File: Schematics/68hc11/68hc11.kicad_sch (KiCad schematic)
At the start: 8 parts, among them U1 MC68HC11A1CC-PLLC, U2 74HC245, U3 74HC373, U4 27C64, U5 HM62256BLP, U6 27C64, U7 MC68B21

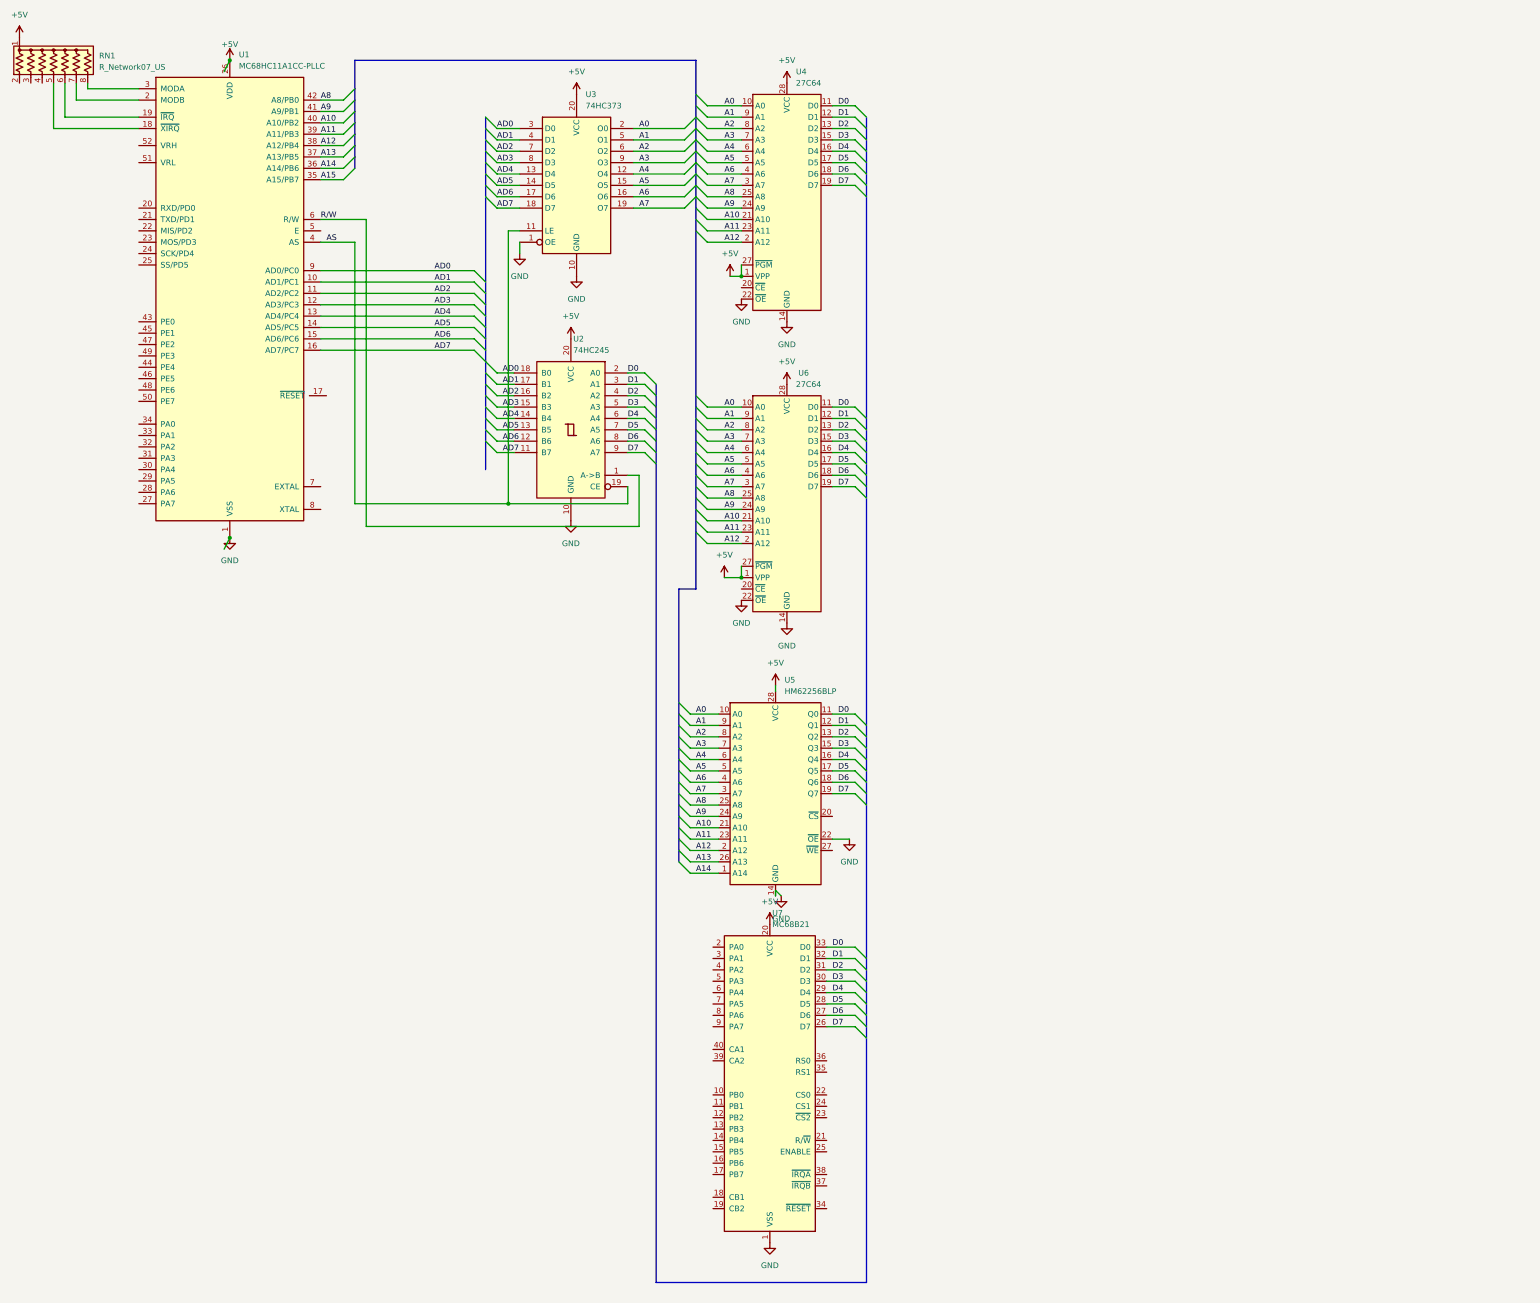
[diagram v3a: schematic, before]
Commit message: Added MAX232 and DB9 for serial comms
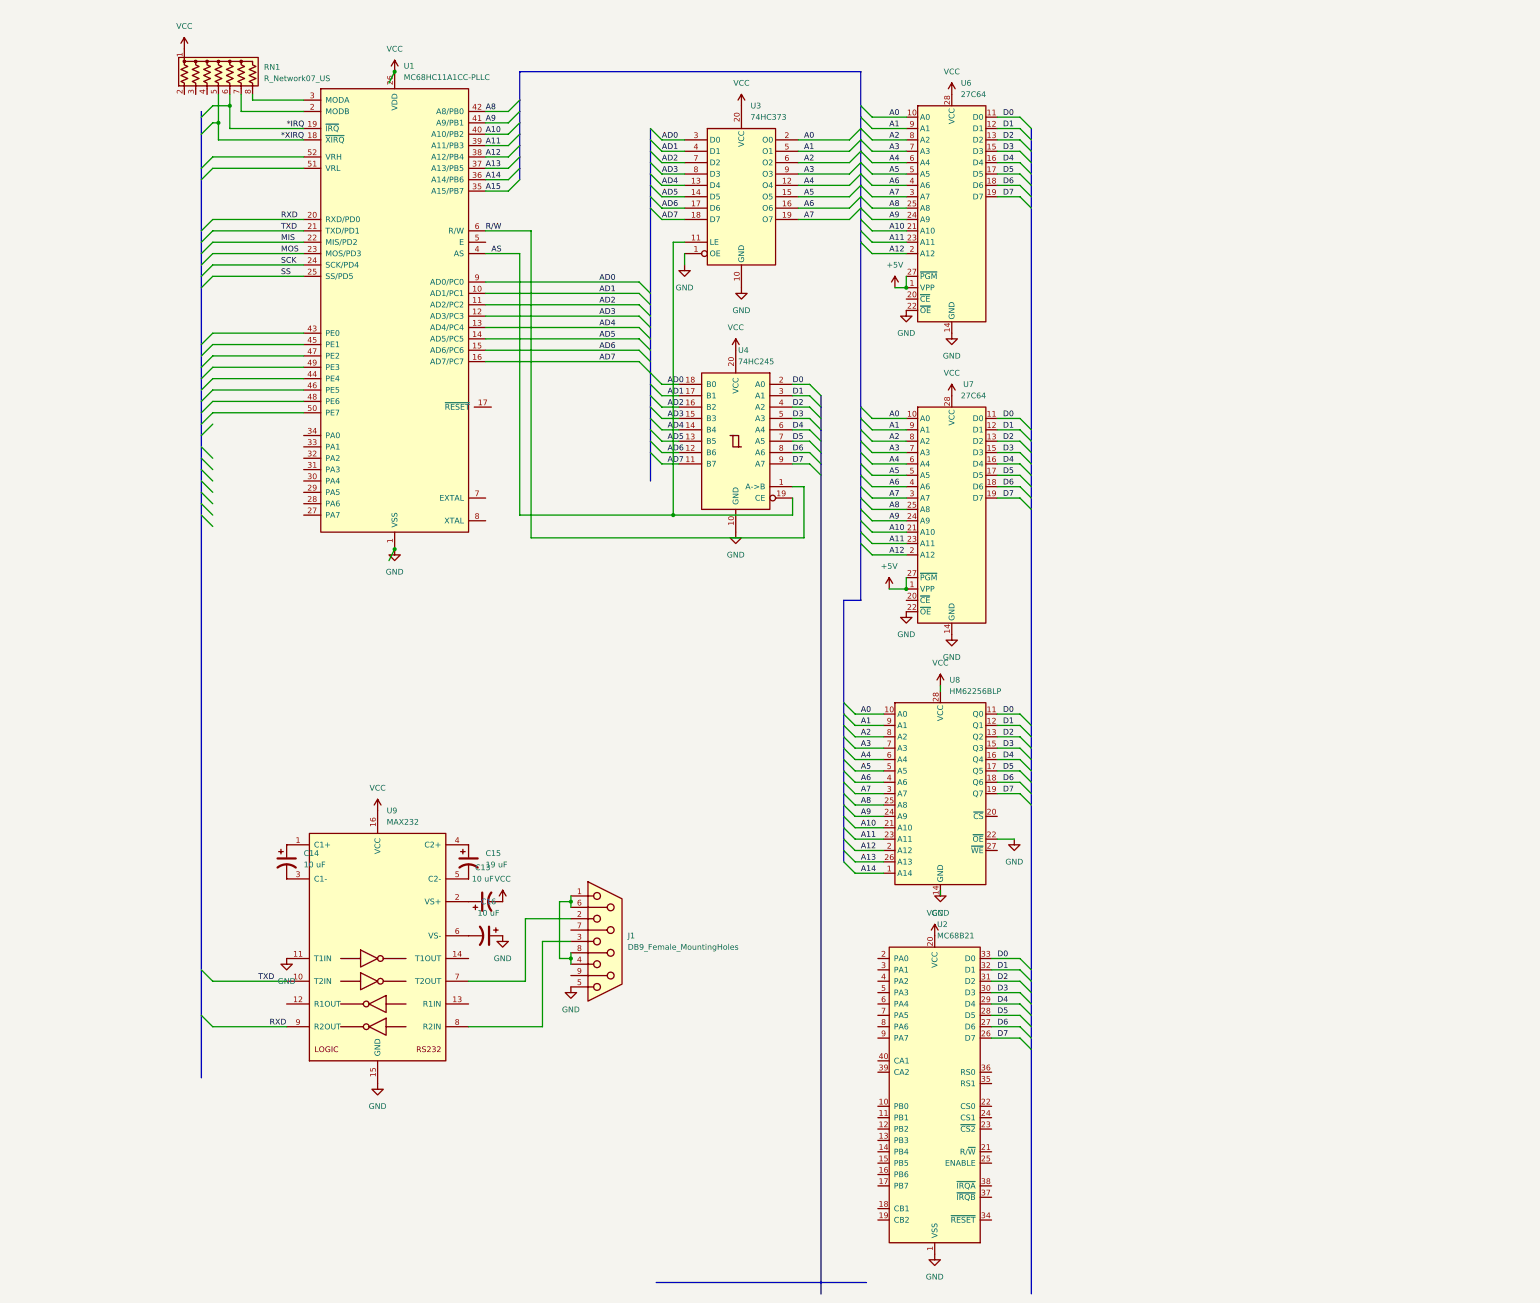
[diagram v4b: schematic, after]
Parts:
- added C13, C14, C16: 10 uF, Capacitor_THT:CP_Radial_D10.0mm_P5.00mm, symbol Device:C_Polarized_US
- added C15: 19 uF, Capacitor_THT:CP_Radial_D10.0mm_P5.00mm, symbol Device:C_Polarized_US
- added J1: DB9_Female_MountingHoles, Connector_Dsub:DSUB-9_Male_Horizontal_P2.77x2.54mm_EdgePinOffset9.40mm, symbol Connector:DB9_Female_MountingHoles
- added U9: MAX232, Package_DIP:DIP-16_W7.62mm_Socket, symbol Interface_UART:MAX232
- U2: renamed from U7; footprint Package_DIP:DIP-40_W15.24mm -> Package_DIP:DIP-40_W15.24mm_Socket
- U6: renamed from U4; footprint Package_DIP:DIP-28_W15.24mm -> Package_DIP:DIP-28_W15.24mm_Socket
- U7: renamed from U6; footprint Package_DIP:DIP-28_W15.24mm -> Package_DIP:DIP-28_W15.24mm_Socket
- U8: renamed from U5; footprint Package_DIP:DIP-28_W15.24mm -> Package_DIP:DIP-28_W15.24mm_Socket
- renumbered U2 to U4
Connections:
- net +5V: no longer RN1.1 (common), U1.26 (VDD), U2.20 (VCC), U3.20 (VCC), U4.20 (VCC), U6.28 (VCC), U7.28 (VCC), U8.28 (VCC)
- net GND: now also C16.1, J1.5, U9.11 (T1IN), U9.15 (GND)
- net *XIRQ: now reaches RN1.5 (R4), U1.18 (~{XIRQ})
- net *IRQ: now reaches RN1.6 (R5), U1.19 (~{IRQ})
- net RXD: now reaches U1.20 (RXD/PD0)
- net RXD: now also U9.9 (R2OUT)
- net TXD: now reaches U1.21 (TXD/PD1)
- net TXD: now also U9.10 (T2IN)
- net MIS: now reaches U1.22 (MIS/PD2)
- net MOS: now reaches U1.23 (MOS/PD3)
- net SCK: now reaches U1.24 (SCK/PD4)
- net SS: now reaches U1.25 (SS/PD5)
- new net: C15.1, U9.4 (C2+)
- new net: C15.2, U9.5 (C2-)
- new net: C14.1, U9.1 (C1+)
- new net: C14.2, U9.3 (C1-)
- new net: J1.1, J1.4, J1.6, J1.8
- new net: J1.2, U9.7 (T2OUT)
- new net: J1.3, U9.8 (R2IN)
- new net: C16.2, U9.6 (VS-)
- new net: C13.1, U9.2 (VS+)
- new net VCC: C13.2, RN1.1 (common), U1.26 (VDD), U2.20 (VCC), U3.20 (VCC), U4.20 (VCC), U6.28 (VCC), U7.28 (VCC), U8.28 (VCC), U9.16 (VCC)
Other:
- moved on the sheet: RN1, U1, U2, U3, U4, U6, U7, U8

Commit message: Added Crystal and some trace routing
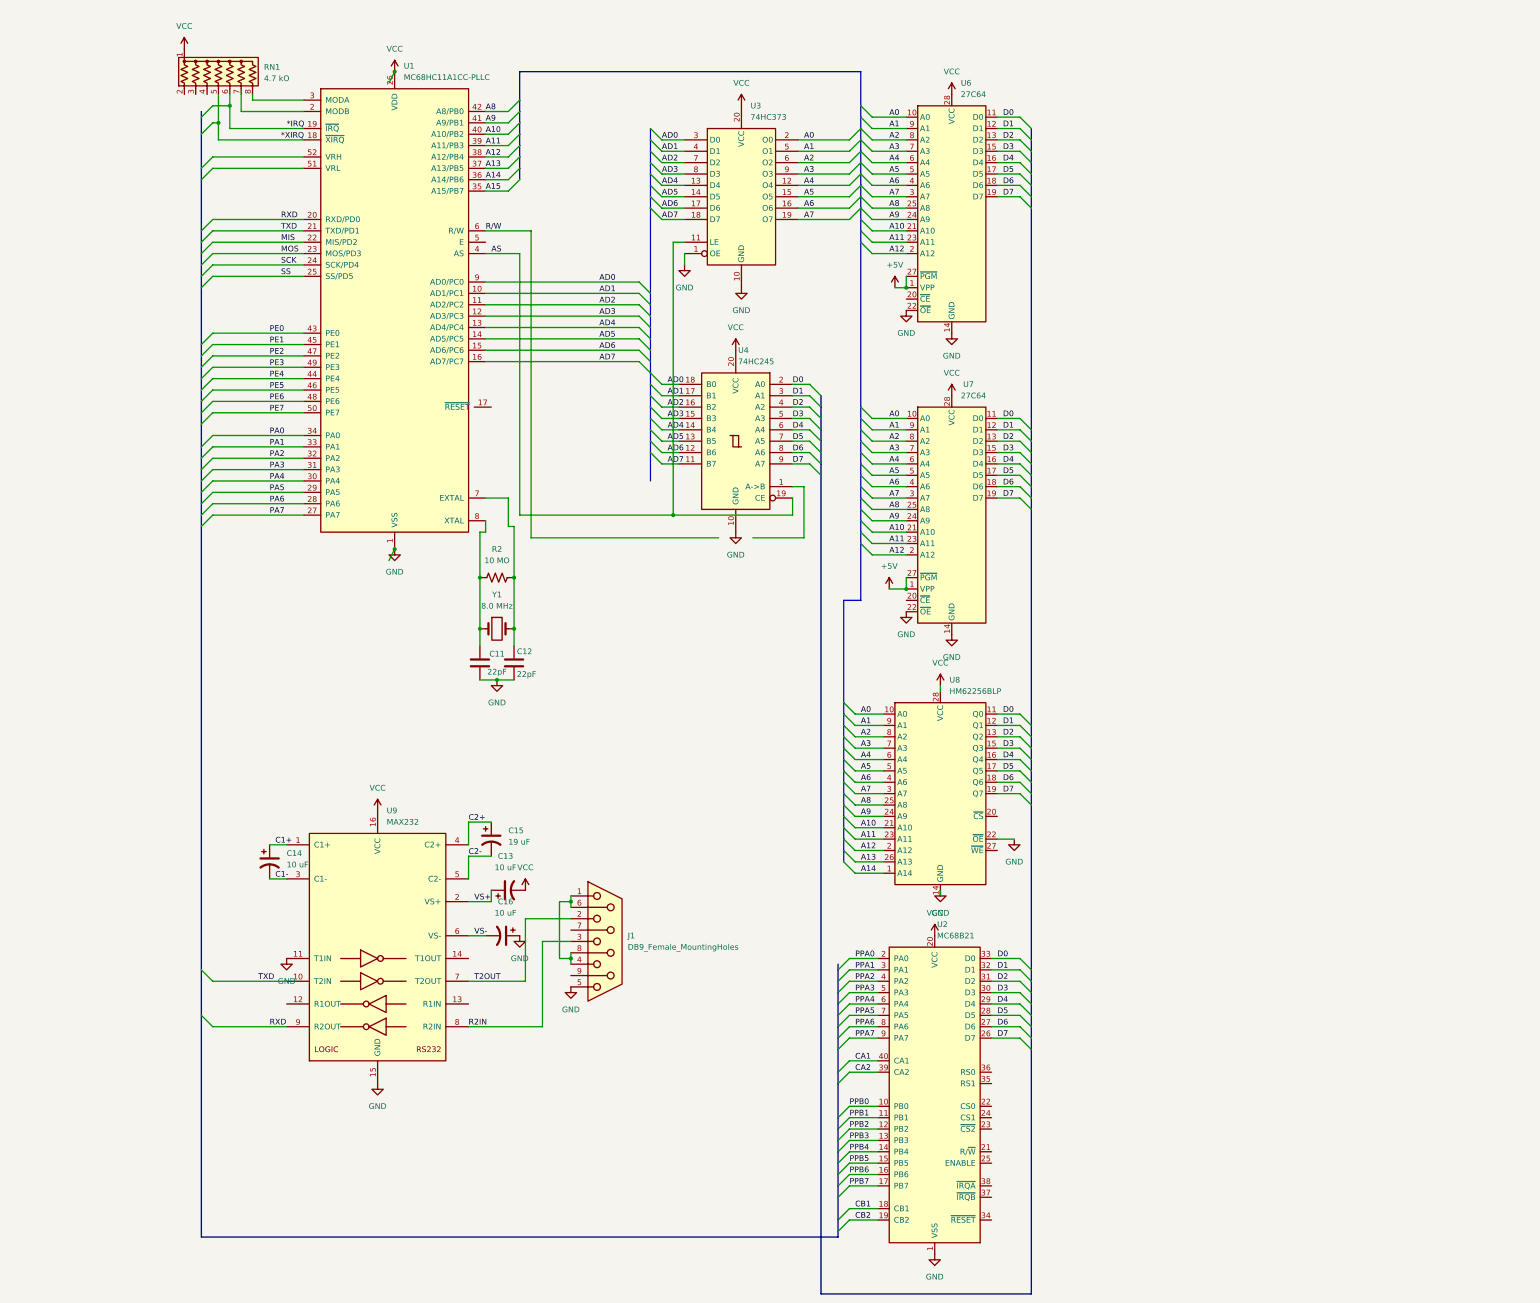
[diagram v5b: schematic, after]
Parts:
- added C11, C12: 22pF, Capacitor_THT:C_Disc_D3.0mm_W1.6mm_P2.50mm, symbol Device:C
- added R2: 10 MO, Resistor_THT:R_Axial_DIN0309_L9.0mm_D3.2mm_P12.70mm_Horizontal, symbol Device:R_US
- added Y1: 8.0 MHz, Crystal:Crystal_HC49-4H_Vertical, symbol Device:Crystal
- C13, C14, C15, C16: footprint Capacitor_THT:CP_Radial_D10.0mm_P5.00mm -> Capacitor_THT:CP_Radial_D5.0mm_P2.00mm
- RN1: value R_Network07_US -> 4.7 kO
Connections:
- net GND: now also C11.2, C12.2
- net R/W: no longer U4.1 (A->B)
- net C2+: now reaches C15.1, U9.4 (C2+)
- net C2-: now reaches C15.2, U9.5 (C2-)
- net C1+: now reaches C14.1, U9.1 (C1+)
- net C1-: now reaches C14.2, U9.3 (C1-)
- net T2OUT: now reaches J1.2, U9.7 (T2OUT)
- net R2IN: now reaches J1.3, U9.8 (R2IN)
- net PA7: now reaches U1.27 (PA7)
- net PA6: now reaches U1.28 (PA6)
- net PA5: now reaches U1.29 (PA5)
- net PA4: now reaches U1.30 (PA4)
- net PA3: now reaches U1.31 (PA3)
- net PA2: now reaches U1.32 (PA2)
- net PA1: now reaches U1.33 (PA1)
- net PA0: now reaches U1.34 (PA0)
- net PE0: now reaches U1.43 (PE0)
- net PE4: now reaches U1.44 (PE4)
- net PE1: now reaches U1.45 (PE1)
- net PE5: now reaches U1.46 (PE5)
- net PE2: now reaches U1.47 (PE2)
- net PE6: now reaches U1.48 (PE6)
- net PE3: now reaches U1.49 (PE3)
- net PE7: now reaches U1.50 (PE7)
- net at U1.7 (EXTAL): now also C12.1, R2.1, Y1.2
- net at U1.8 (XTAL): now also C11.1, R2.2, Y1.1
- net PPB0: now reaches U2.10 (PB0)
- net PPB1: now reaches U2.11 (PB1)
- net PPB2: now reaches U2.12 (PB2)
- net PPB3: now reaches U2.13 (PB3)
- net PPB4: now reaches U2.14 (PB4)
- net PPB5: now reaches U2.15 (PB5)
- net PPB6: now reaches U2.16 (PB6)
- net PPB7: now reaches U2.17 (PB7)
- net CB1: now reaches U2.18 (CB1)
- net CB2: now reaches U2.19 (CB2)
- net PPA0: now reaches U2.2 (PA0)
- net PPA1: now reaches U2.3 (PA1)
- net CA2: now reaches U2.39 (CA2)
- net PPA2: now reaches U2.4 (PA2)
- net CA1: now reaches U2.40 (CA1)
- net PPA3: now reaches U2.5 (PA3)
- net PPA4: now reaches U2.6 (PA4)
- net PPA5: now reaches U2.7 (PA5)
- net PPA6: now reaches U2.8 (PA6)
- net PPA7: now reaches U2.9 (PA7)
- net VS-: now reaches C16.2, U9.6 (VS-)
- net VS+: now reaches C13.1, U9.2 (VS+)
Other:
- moved on the sheet: C13, C14, C15, C16

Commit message: Added low power reset and cleaned up busses
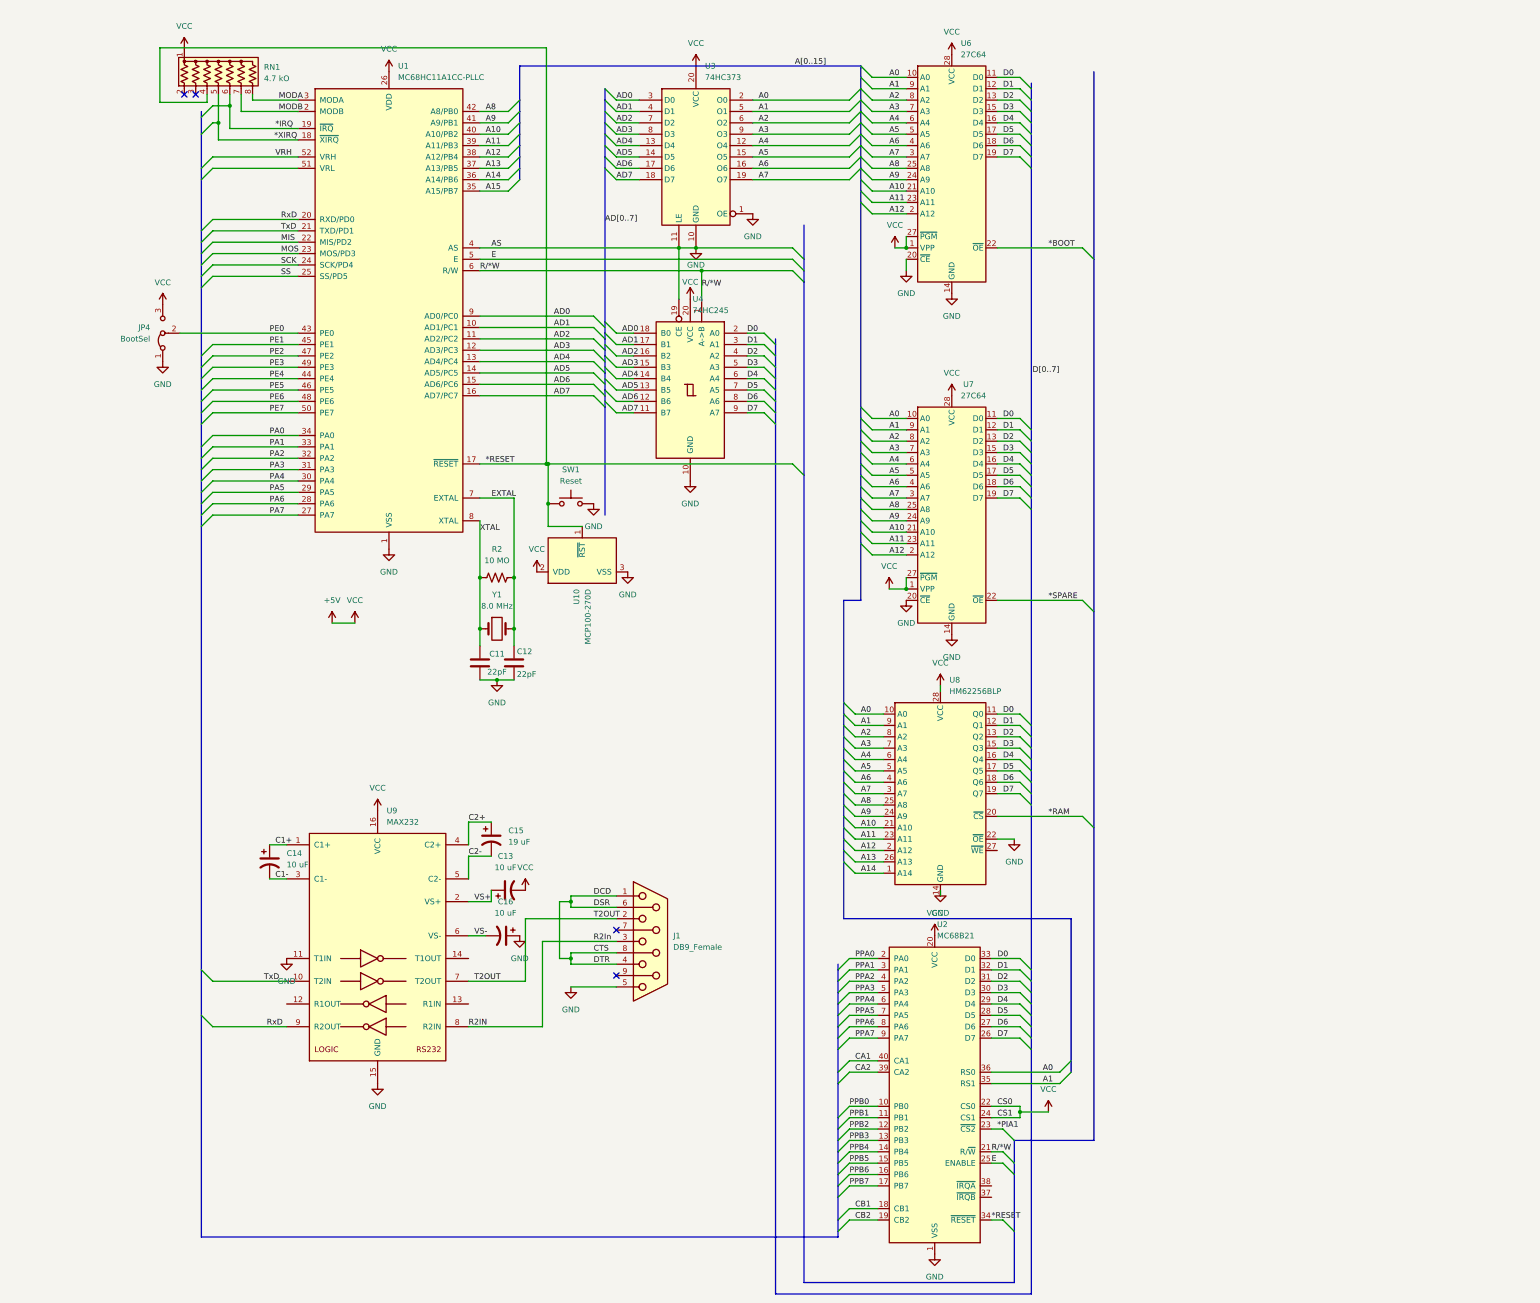
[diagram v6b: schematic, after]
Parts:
- added JP4: BootSel, Connector_PinHeader_1.00mm:PinHeader_1x03_P1.00mm_Vertical, symbol Jumper:Jumper_3_Bridged12
- added SW1: Reset, Button_Switch_THT:SW_PUSH_6mm, symbol Switch:SW_Push
- added U10: MCP100-270D, Package_TO_SOT_THT:TO-92, symbol Power_Supervisor:MCP100-270D
- J1: value DB9_Female_MountingHoles -> DB9_Female
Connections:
- net AS is gone; now on net GND: U1.4 (AS), U3.11 (LE), U4.19 (CE)
- net R/W is gone; now on net R/*W: U1.6 (R/W)
- net VCC is gone; now on net +5V: C13.2, RN1.1 (common), U1.26 (VDD), U2.20 (VCC), U3.20 (VCC), U4.20 (VCC), U6.28 (VCC), U7.28 (VCC), U8.28 (VCC), U9.16 (VCC)
- net +5V: now also U2.22 (CS0), U2.24 (CS1), JP4.3 (B), U10.2 (VDD)
- net A0: now also U2.36 (RS0)
- net A1: now also U2.35 (RS1)
- net GND: now also U6.20 (~{CE}), U7.20 (~{CE}), JP4.1 (A), SW1.2, U10.3 (VSS); no longer U6.22 (~{OE}), U7.22 (~{OE})
- net PE0: now also JP4.2 (C)
- net *RESET: now reaches RN1.4 (R3)
- net *RESET: now also U1.17 (~{RESET}), U2.34 (~{RESET}), SW1.1, U10.1 (~{RST})
- net MODB: now reaches RN1.7 (R6), U1.2 (MODB)
- net MODA: now reaches RN1.8 (R7), U1.3 (MODA)
- net XTAL: now reaches C11.1, R2.2, U1.8 (XTAL), Y1.1
- net EXTAL: now reaches C12.1, R2.1, U1.7 (EXTAL), Y1.2
- net *RAM: now reaches U8.20 (~{CS})
- net CTS: now reaches J1.1, J1.4, J1.6, J1.8
- net E: now reaches U1.5 (E)
- net E: now also U2.25 (ENABLE)
- net VRH: now reaches U1.52 (VRH)
- net R/*W: now reaches U2.21 (R/~{W})
- net R/*W: now also U4.1 (A->B)
- net *PIA1: now reaches U2.23 (~{CS2})
- net RXD renamed RxD
- net TXD renamed TxD
- new net *BOOT: U6.22 (~{OE})
- new net *SPARE: U7.22 (~{OE})
- no-connect marks 0 -> 4
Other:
- moved on the sheet: J1, U1, U3, U4, U6
